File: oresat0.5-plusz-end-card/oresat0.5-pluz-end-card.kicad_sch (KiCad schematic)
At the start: 38 parts, among them J1 J-SAMTEC-TFM-120-01-L-D-RA, J2 Harwin M55-7101242R, J3 Harwin M55-7101242R, J4 Harwin M55-7101242R, J5 Harwin M55-7101242R, J6 Conn_Coaxial

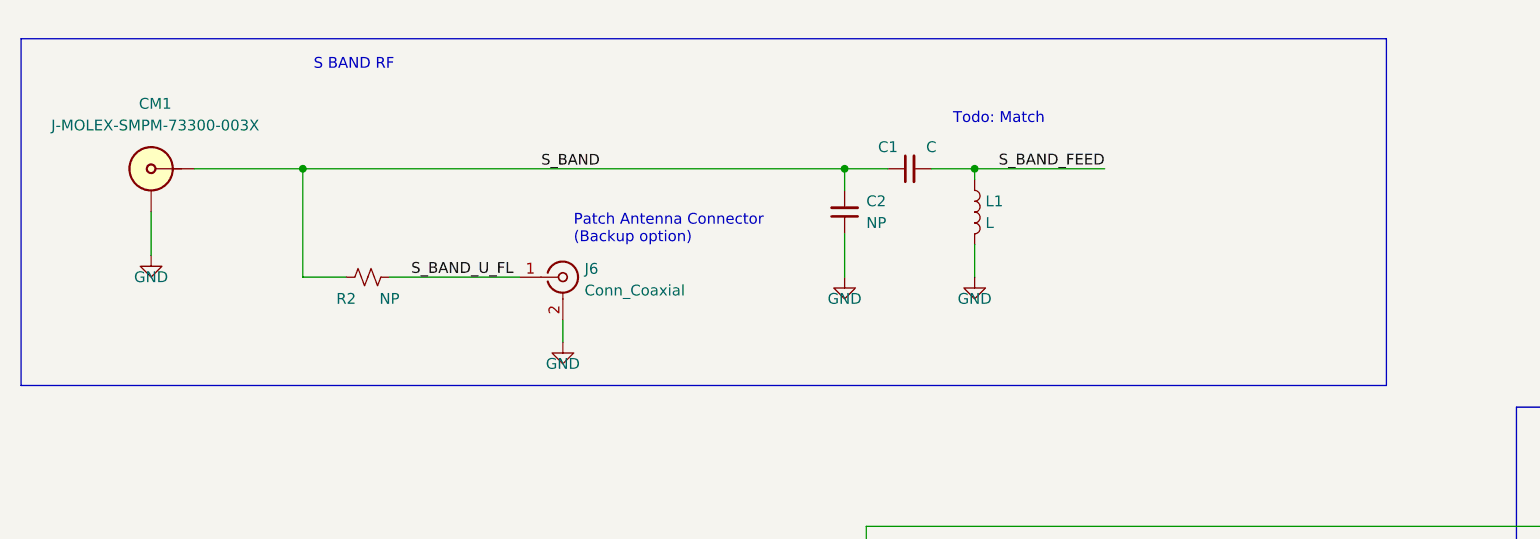
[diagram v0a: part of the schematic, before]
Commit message: Updated helical matching network components and values
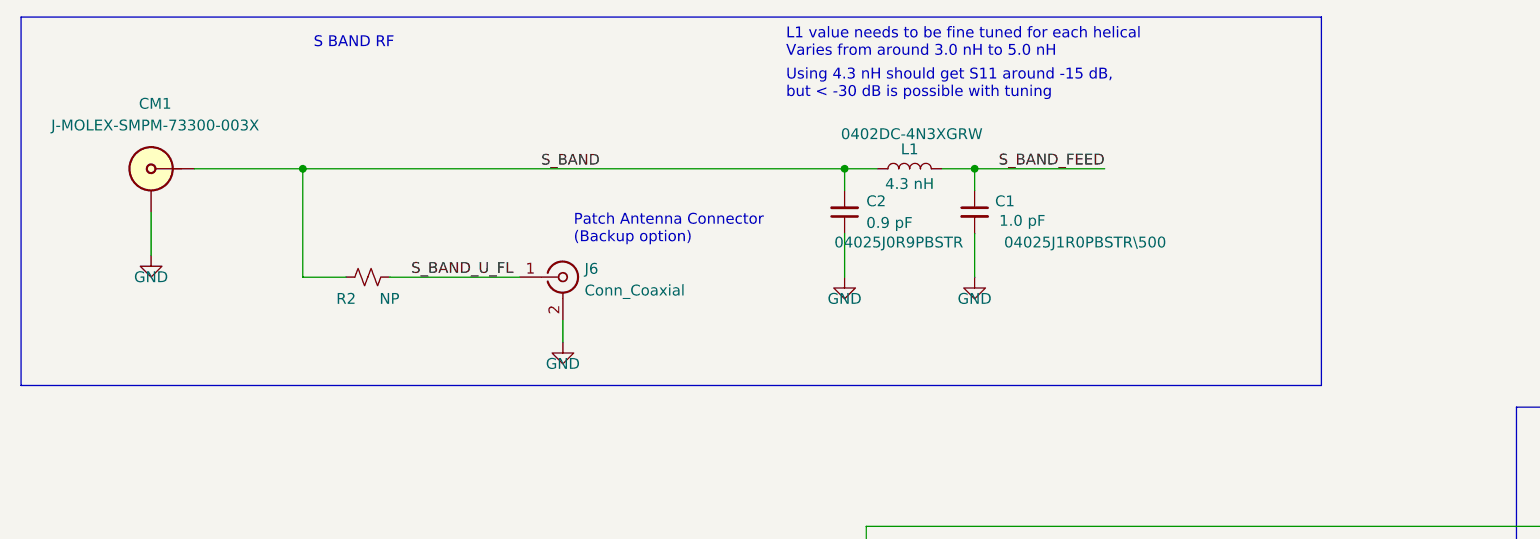
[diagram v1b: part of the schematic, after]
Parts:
- C1: value C -> 1.0 pF; MPN (none) -> 04025J1R0PBSTR\500
- C2: value NP -> 0.9 pF; MPN (none) -> 04025J0R9PBSTR
- L1: value L -> 4.3 nH; MPN (none) -> 0402DC-4N3XGRW
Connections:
- net GND: now also C1.2; no longer L1.2
- net S_BAND: now also L1.1; no longer C1.1
- net S_BAND_FEED: now also C1.1, L1.2; no longer C1.2, L1.1
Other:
- note added: "L1 value needs to be fine tuned for each helical Varies from around 3.0 nH to 5.0 nH"
- note added: "Using 4.3 nH should get S11 around -15 dB, but < -30 dB is possible with tuning"
- note removed: "Todo: Match"
- moved on the sheet: C1, L1
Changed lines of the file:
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@@
 	)
 	(junction
-		(at 144.78 35.56)
-		(diameter 0)
-		(color 0 0 0 0)
-	)
-	(junction
 		(at 175.26 162.56)
 		(diameter 0)
@@
 	)
 	(junction
-		(at 160.02 35.56)
+		(at 144.78 35.56)
 		(diameter 0)
 		(color 0 0 0 0)
@@
 	)
 	(junction
+		(at 160.02 35.56)
+		(diameter 0)
+		(color 0 0 0 0)
+	)
+	(junction
 		(at 205.74 160.02)
 		(diameter 0)
@@
 	(wire
 		(pts
-			(xy 160.02 44.45) (xy 160.02 48.26)
+			(xy 160.02 43.18) (xy 160.02 48.26)
 		)
 		(stroke
@@
 	(polyline
 		(pts
-			(xy 48.26 20.32) (xy 48.26 60.96)
+			(xy 48.26 17.78) (xy 48.26 60.96)
 		)
 		(stroke
@@
 	(polyline
 		(pts
-			(xy 208.28 60.96) (xy 48.26 60.96)
-		)
-		(stroke
-			(width 0)
-			(type default)
-		)
-	)
-	(wire
-		(pts
-			(xy 154.94 35.56) (xy 160.02 35.56)
+			(xy 200.66 60.96) (xy 48.26 60.96)
 		)
 		(stroke
@@
 	(polyline
 		(pts
-			(xy 208.28 20.32) (xy 208.28 60.96)
+			(xy 200.66 17.78) (xy 200.66 60.96)
 		)
 		(stroke
@@
 	(polyline
 		(pts
-			(xy 48.26 20.32) (xy 208.28 20.32)
+			(xy 48.26 17.78) (xy 200.66 17.78)
 		)
 		(stroke
@@
 	(wire
 		(pts
-			(xy 160.02 36.83) (xy 160.02 35.56)
+			(xy 160.02 35.56) (xy 160.02 38.1)
 		)
 		(stroke
@@
 		)
 	)
+	(wire
+		(pts
+			(xy 144.78 35.56) (xy 148.59 35.56)
+		)
+		(stroke
+			(width 0)
+			(type default)
+		)
+	)
 	(polyline
 		(pts
@@
 	(wire
 		(pts
+			(xy 156.21 35.56) (xy 160.02 35.56)
+		)
+		(stroke
+			(width 0)
+			(type default)
+		)
+	)
+	(wire
+		(pts
 			(xy 74.93 101.6) (xy 152.4 101.6)
 		)
@@
 		)
 	)
-	(wire
-		(pts
-			(xy 144.78 35.56) (xy 149.86 35.56)
-		)
-		(stroke
-			(width 0)
-			(type default)
-		)
-	)
 	(text "TO +Z END CAP"
 		(exclude_from_sim no)
@@
 		)
 	)
-	(text "Todo: Match"
+	(text "L1 value needs to be fine tuned for each helical\nVaries from around 3.0 nH to 5.0 nH"
 		(exclude_from_sim no)
-		(at 157.48 30.48 0)
+		(at 137.922 22.606 0)
 		(effects
 			(font
@@
 		)
 	)
+	(text "Using 4.3 nH should get S11 around -15 dB, \nbut < -30 dB is possible with tuning"
+		(exclude_from_sim no)
+		(at 137.922 27.432 0)
+		(effects
+			(font
+				(size 1.27 1.27)
+			)
+			(justify left bottom)
+		)
+	)
 	(text "-Y"
 		(exclude_from_sim no)
@@
 	(text "S BAND RF"
 		(exclude_from_sim no)
-		(at 82.55 24.13 0)
+		(at 82.55 21.59 0)
 		(effects
 			(font
@@
 		(on_board yes)
 		(dnp no)
-		(fields_autoplaced yes)
 		(property "Reference" "C2"
-			(at 147.32 39.3636 0)
+			(at 147.32 39.3635 0)
 			(effects
 				(font
@@
 			)
 		)
-		(property "Value" "NP"
-			(at 147.32 41.9036 0)
+		(property "Value" "0.9 pF"
+			(at 147.32 41.9035 0)
 			(effects
 				(font
@@
 			)
 		)
+		(property "MPN" "04025J0R9PBSTR"
+			(at 151.13 44.196 0)
+			(effects
+				(font
+					(size 1.27 1.27)
+				)
+			)
+		)
 		(pin "1"
 		)
@@
 	(symbol
 		(lib_id "Device:C_Small")
-		(at 152.4 35.56 90)
+		(at 160.02 40.64 0)
 		(unit 1)
 		(exclude_from_sim no)
@@
 		(dnp no)
 		(property "Reference" "C1"
-			(at 149.86 33.02 90)
+			(at 163.576 39.37 0)
 			(effects
 				(font
@@
 			)
 		)
-		(property "Value" "C"
-			(at 154.94 33.02 90)
+		(property "Value" "1.0 pF"
+			(at 165.608 41.656 0)
 			(effects
 				(font
@@
 		)
 		(property "Footprint" "Capacitor_SMD:C_0402_1005Metric"
-			(at 152.4 35.56 0)
+			(at 160.02 40.64 0)
 			(effects
 				(font
@@
 		)
 		(property "Datasheet" "~"
-			(at 152.4 35.56 0)
+			(at 160.02 40.64 0)
 			(effects
 				(font
@@
 		)
 		(property "Description" ""
-			(at 152.4 35.56 0)
+			(at 160.02 40.64 0)
 			(effects
 				(font
@@
 			)
 		)
+		(property "MPN" "04025J1R0PBSTR\\500"
+			(at 172.974 44.196 0)
+			(effects
+				(font
+					(size 1.27 1.27)
+				)
+			)
+		)
 		(pin "1"
 		)
@@
 	(symbol
 		(lib_id "Device:L")
-		(at 160.02 40.64 0)
+		(at 152.4 35.56 90)
 		(unit 1)
 		(exclude_from_sim no)
@@
 		(on_board yes)
 		(dnp no)
-		(fields_autoplaced yes)
 		(property "Reference" "L1"
-			(at 161.29 39.3699 0)
+			(at 152.4 33.274 90)
 			(effects
 				(font
 					(size 1.27 1.27)
 				)
-				(justify left)
 			)
 		)
-		(property "Value" "L"
-			(at 161.29 41.9099 0)
+		(property "Value" "4.3 nH"
+			(at 152.4 37.338 90)
 			(effects
 				(font
 					(size 1.27 1.27)
 				)
-				(justify left)
 			)
 		)
 		(property "Footprint" "Inductor_SMD:L_0402_1005Metric"
-			(at 160.02 40.64 0)
+			(at 152.4 35.56 0)
 			(effects
 				(font
@@
 		)
 		(property "Datasheet" "~"
-			(at 160.02 40.64 0)
+			(at 152.4 35.56 0)
 			(effects
 				(font
@@
 		)
 		(property "Description" ""
-			(at 160.02 40.64 0)
+			(at 152.4 35.56 0)
 			(effects
 				(font
@@
 			)
 		)
+		(property "MPN" "0402DC-4N3XGRW"
+			(at 152.654 31.496 90)
+			(effects
+				(font
+					(size 1.27 1.27)
+				)
+			)
+		)

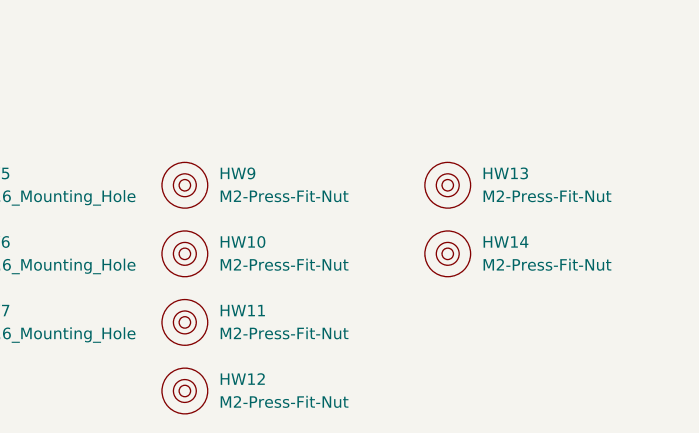
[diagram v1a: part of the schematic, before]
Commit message: Updated hole positions for single door deployer. TODO: fix weird net class errors that shouldn't exist.
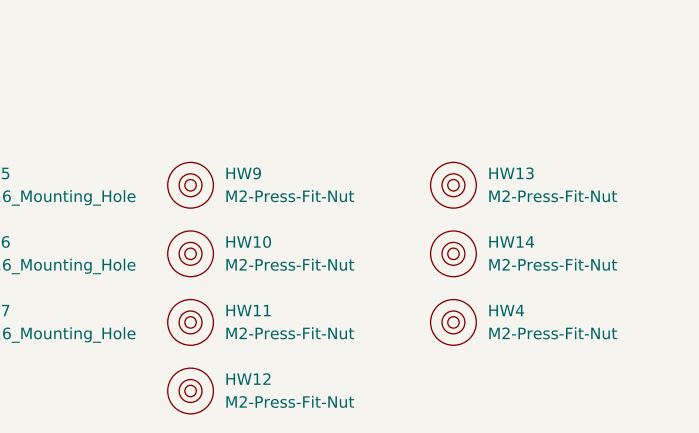
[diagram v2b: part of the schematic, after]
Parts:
- added HW4: M2-Press-Fit-Nut, oresat-misc:M2-Press-Fit-Nut, symbol oresat-misc:M2-Press-Fit-Nut
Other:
- moved on the sheet: HW10, HW11, HW12, HW13, HW14, HW9
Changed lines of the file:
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@@
 	(title_block
 		(title "+Z End Card w/ Turnstile")
-		(date "2024-02-26")
-		(rev "1.2")
+		(date "2024-08-20")
+		(rev "1.4")
 	)
 	(junction
@@
 			)
 		)
-		(property "Datasheet" " ~"
+		(property "Datasheet" "~"
 			(at 111.76 48.26 0)
 			(effects
@@
 	(symbol
 		(lib_id "oresat-misc:M2-Press-Fit-Nut")
-		(at 249.555 250.19 0)
+		(at 250.19 250.19 0)
 		(unit 1)
 		(exclude_from_sim no)
@@
 		(fields_autoplaced yes)
 		(property "Reference" "HW12"
-			(at 253.365 248.9199 0)
+			(at 254 248.9199 0)
 			(effects
 				(font
@@
 		)
 		(property "Value" "M2-Press-Fit-Nut"
-			(at 253.365 251.4599 0)
+			(at 254 251.4599 0)
 			(effects
 				(font
@@
 		)
 		(property "Footprint" "oresat-misc:M2-Press-Fit-Nut"
-			(at 249.555 254.635 0)
+			(at 250.19 254.635 0)
 			(effects
 				(font
@@
 		)
 		(property "Datasheet" ""
-			(at 249.555 250.19 0)
+			(at 250.19 250.19 0)
 			(effects
 				(font
@@
 		)
 		(property "Description" ""
-			(at 249.555 250.19 0)
+			(at 250.19 250.19 0)
 			(effects
 				(font
@@
 	(symbol
 		(lib_id "oresat-misc:M2-Press-Fit-Nut")
-		(at 278.765 234.95 0)
+		(at 279.4 234.95 0)
 		(unit 1)
 		(exclude_from_sim no)
@@
 		(fields_autoplaced yes)
 		(property "Reference" "HW14"
-			(at 282.575 233.68 0)
+			(at 283.21 233.68 0)
 			(effects
 				(font
@@
 		)
 		(property "Value" "M2-Press-Fit-Nut"
-			(at 282.575 236.22 0)
+			(at 283.21 236.22 0)
 			(effects
 				(font
@@
 		)
 		(property "Footprint" "oresat-misc:M2-Press-Fit-Nut"
-			(at 278.765 239.395 0)
+			(at 279.4 239.395 0)
 			(effects
 				(font
@@
 		)
 		(property "Datasheet" ""
-			(at 278.765 234.95 0)
+			(at 279.4 234.95 0)
 			(effects
 				(font
@@
 		)
 		(property "Description" ""
-			(at 278.765 234.95 0)
+			(at 279.4 234.95 0)
 			(effects
 				(font
@@
 	(symbol
 		(lib_id "oresat-misc:M2-Press-Fit-Nut")
-		(at 249.555 234.95 0)
+		(at 250.19 234.95 0)
 		(unit 1)
 		(exclude_from_sim no)
@@
 		(dnp no)
 		(property "Reference" "HW10"
-			(at 253.365 233.6799 0)
+			(at 254 233.6799 0)
 			(effects
 				(font
@@
 		)
 		(property "Value" "M2-Press-Fit-Nut"
-			(at 253.365 236.22 0)
+			(at 254 236.22 0)
 			(effects
 				(font
@@
 		)
 		(property "Footprint" "oresat-misc:M2-Press-Fit-Nut"
-			(at 249.555 239.395 0)
+			(at 250.19 239.395 0)
 			(effects
 				(font
@@
 		)
 		(property "Datasheet" ""
-			(at 249.555 234.95 0)
+			(at 250.19 234.95 0)
 			(effects
 				(font
@@
 		)
 		(property "Description" ""
-			(at 249.555 234.95 0)
+			(at 250.19 234.95 0)
 			(effects
 				(font
@@
 	)
 	(symbol
+		(lib_id "oresat-misc:M2-Press-Fit-Nut")
+		(at 279.4 242.57 0)
+		(unit 1)
+		(exclude_from_sim no)
+		(in_bom yes)
+		(on_board yes)
+		(dnp no)
+		(fields_autoplaced yes)
+		(property "Reference" "HW4"
+			(at 283.21 241.3 0)
+			(effects
+				(font
+					(size 1.27 1.27)
+				)
+				(justify left)
+			)
+		)
+		(property "Value" "M2-Press-Fit-Nut"
+			(at 283.21 243.84 0)
+			(effects
+				(font
+					(size 1.27 1.27)
+				)
+				(justify left)
+			)
+		)
+		(property "Footprint" "oresat-misc:M2-Press-Fit-Nut"
+			(at 279.4 247.015 0)
+			(effects
+				(font
+					(size 1.27 1.27)
+				)
+				(hide yes)
+			)
+		)
+		(property "Datasheet" ""
+			(at 279.4 242.57 0)
+			(effects
+				(font
+					(size 1.27 1.27)
+				)
+				(hide yes)
+			)
+		)
+		(property "Description" ""
+			(at 279.4 242.57 0)
+			(effects
+				(font
+					(size 1.27 1.27)
+				)
+				(hide yes)
+			)
+		)
+		(instances
+			(project "oresat0.5-pluz-end-card"
+				(path "/f7595184-4323-4ed9-b19e-5e32e3c6e76f"
+					(reference "HW4")
+					(unit 1)
+				)
+			)
+		)
+	)
+	(symbol
 		(lib_id "oresat-misc:Test-Point-0.75mm-th")
 		(at 167.64 165.1 270)
@@
 	(symbol
 		(lib_id "oresat-misc:M2-Press-Fit-Nut")
-		(at 278.765 227.33 0)
+		(at 279.4 227.33 0)
 		(unit 1)
 		(exclude_from_sim no)
@@
 		(fields_autoplaced yes)
 		(property "Reference" "HW13"
-			(at 282.575 226.06 0)
+			(at 283.21 226.06 0)
 			(effects
 				(font
@@
 		)
 		(property "Value" "M2-Press-Fit-Nut"
-			(at 282.575 228.6 0)
+			(at 283.21 228.6 0)
 			(effects
 				(font
@@
 		)
 		(property "Footprint" "oresat-misc:M2-Press-Fit-Nut"
-			(at 278.765 231.775 0)
+			(at 279.4 231.775 0)
 			(effects
 				(font
@@
 		)
 		(property "Datasheet" ""
-			(at 278.765 227.33 0)
+			(at 279.4 227.33 0)
 			(effects
 				(font
@@
 		)
 		(property "Description" ""
-			(at 278.765 227.33 0)
+			(at 279.4 227.33 0)
 			(effects
 				(font
@@
 	(symbol
 		(lib_id "oresat-misc:M2-Press-Fit-Nut")
-		(at 249.555 227.33 0)
+		(at 250.19 227.33 0)
 		(unit 1)
 		(exclude_from_sim no)
@@
 		(fields_autoplaced yes)
 		(property "Reference" "HW9"
-			(at 253.365 226.0599 0)
+			(at 254 226.0599 0)
 			(effects
 				(font
@@
 		)
 		(property "Value" "M2-Press-Fit-Nut"
-			(at 253.365 228.5999 0)
+			(at 254 228.5999 0)
 			(effects
 				(font
@@
 		)
 		(property "Footprint" "oresat-misc:M2-Press-Fit-Nut"
-			(at 249.555 231.775 0)
+			(at 250.19 231.775 0)
 			(effects
 				(font
@@
 		)
 		(property "Datasheet" ""
-			(at 249.555 227.33 0)
+			(at 250.19 227.33 0)
 			(effects
 				(font
@@
 		)
 		(property "Description" ""
-			(at 249.555 227.33 0)
+			(at 250.19 227.33 0)
 			(effects
 				(font
@@
 	(symbol
 		(lib_id "oresat-misc:M2-Press-Fit-Nut")
-		(at 249.555 242.57 0)
+		(at 250.19 242.57 0)
 		(unit 1)
 		(exclude_from_sim no)
@@
 		(dnp no)
 		(property "Reference" "HW11"
-			(at 253.365 241.2999 0)
+			(at 254 241.2999 0)
 			(effects
 				(font
@@
 		)
 		(property "Value" "M2-Press-Fit-Nut"
-			(at 253.365 243.84 0)
+			(at 254 243.84 0)
 			(effects
 				(font
@@
 		)
 		(property "Footprint" "oresat-misc:M2-Press-Fit-Nut"
-			(at 249.555 247.015 0)
+			(at 250.19 247.015 0)
 			(effects
 				(font
@@
 		)
 		(property "Datasheet" ""
-			(at 249.555 242.57 0)
+			(at 250.19 242.57 0)
 			(effects
 				(font
@@
 		)
 		(property "Description" ""
-			(at 249.555 242.57 0)
+			(at 250.19 242.57 0)
 			(effects
 				(font

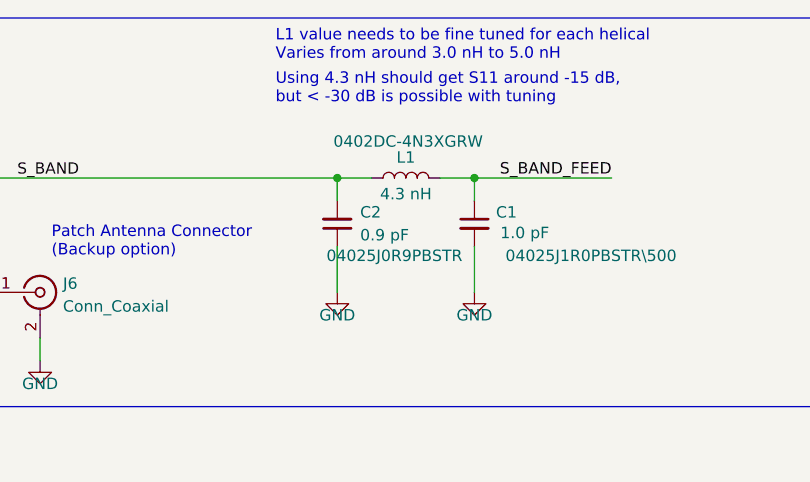
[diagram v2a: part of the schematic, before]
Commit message: added components in symbol field for BOM
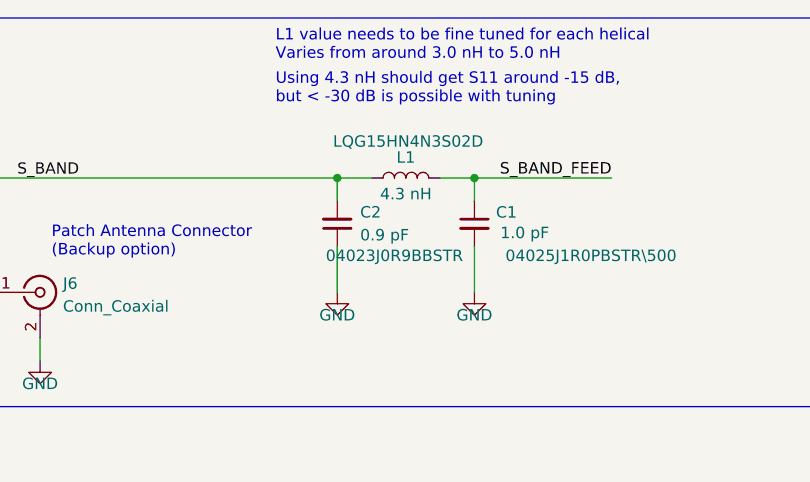
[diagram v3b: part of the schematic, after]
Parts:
- C1: DIST (none) -> DigiKey; DPN (none) -> 478-04025J1R0PBSTR\500CT-ND; MFR (none) -> KYOCERA AVX
- C2: DIST (none) -> DigiKey; DPN (none) -> 478-04023J0R9BBSTRCT-ND; MFR (none) -> KYOCERA AVX; MPN 04025J0R9PBSTR -> 04023J0R9BBSTR
- CF1: DIST (none) -> DigiKey; DPN (none) -> 952-3851-1-ND; MFR (none) -> Harwin Inc.; MPN (none) -> M55-6021242R
- CM1: DIST (none) -> DigiKey; DPN (none) -> WM10772-ND; MFR (none) -> DigiKey; MPN (none) -> 952-3851-1-ND
- J1: DIST (none) -> DigiKey; DPN (none) -> SAM10145-ND; MFR (none) -> Samtec; MPN (none) -> TFM-120-01-L-D-RA
- J2, J3, J4, J5: DIST (none) -> DigiKey; DPN (none) -> 952-3891-1-ND; MFR (none) -> Harwin Inc.; MPN (none) -> M55-7101242R
- J6: DIST (none) -> DigiKey; DPN (none) -> H11891CT-ND; MFR (none) -> Hirose; MPN (none) -> U.FL-R-SMT-1(10)
- L1: DIST (none) -> DigiKey; DPN (none) -> 490-6563-1-ND; MFR (none) -> Murata Electronics; MPN 0402DC-4N3XGRW -> LQG15HN4N3S02D
- R1: DIST (none) -> DigiKey; DPN (none) -> 749-PAC100007508FA1000TB-ND; MFR (none) -> Vishay Beyschlag/Draloric/BC Components; MPN (none) -> PAC100007508FA1000
- R2: DIST (none) -> Digikey; DPN (none) -> RMCF0603ZT0R00CT-ND; MFR (none) -> Stackpole Electronics Inc; MPN (none) -> RMCF0603ZT0R00

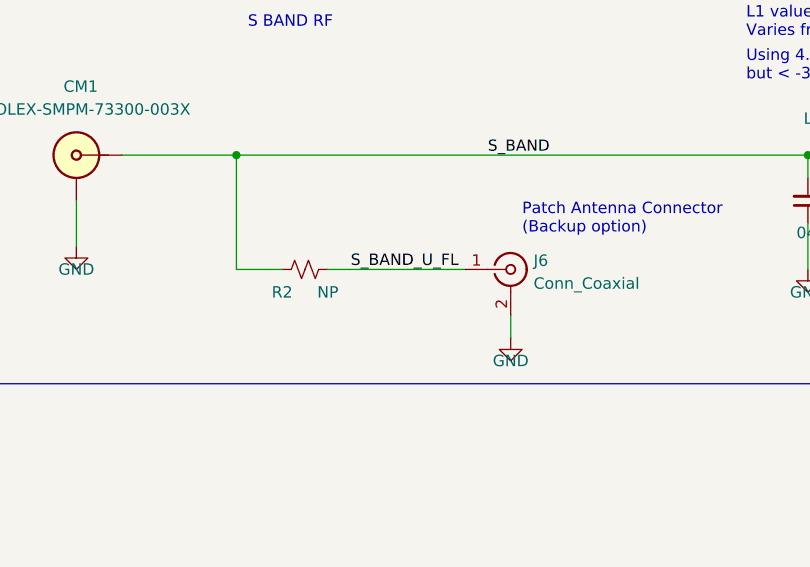
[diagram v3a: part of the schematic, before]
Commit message: R2 and J6 excluded from BOM and set as DNP
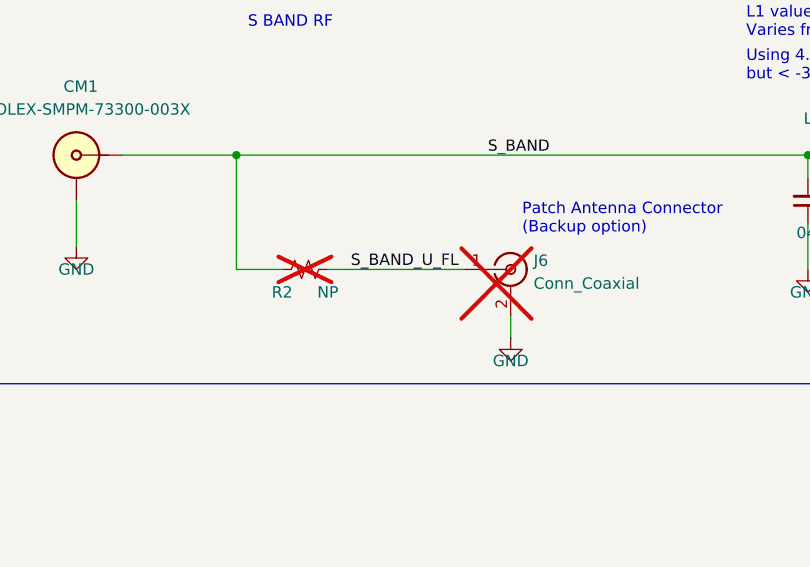
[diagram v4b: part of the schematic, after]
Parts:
- J6, R2: now not fitted; now left out of the parts list
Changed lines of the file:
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@@
 		(unit 1)
 		(exclude_from_sim no)
-		(in_bom yes)
-		(on_board yes)
-		(dnp no)
+		(in_bom no)
+		(on_board yes)
+		(dnp yes)
 		(fields_autoplaced yes)
 		(property "Reference" "J6"
@@
 		(unit 1)
 		(exclude_from_sim no)
-		(in_bom yes)
-		(on_board yes)
-		(dnp no)
+		(in_bom no)
+		(on_board yes)
+		(dnp yes)
 		(property "Reference" "R2"
 			(at 86.36 50.8 90)
